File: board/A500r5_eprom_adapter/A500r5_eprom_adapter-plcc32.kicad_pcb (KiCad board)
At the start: 2 copper layers, 10 parts, among them J1 PWR, J2 A18 Selector, J3 A19 Selector, U1 27C400-A500, U2 27C080-L, U3 27C080-L

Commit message: More PLCC32 changes
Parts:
- U2: moved to F.Cu
- moved U2 17.8 mm to (141.0, 96.5)
- moved U3 14.2 mm to (141.0, 96.5)
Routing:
- net VCC: track 0.00 -> 25.7 mm, vias 0 -> 1
- net /A7: track 0.00 -> 16.3 mm, vias 0 -> 1
- net /A14: track 0.00 -> 15.6 mm, vias 0 -> 1
- net /A16: track 0.00 -> 15.4 mm, vias 0 -> 1
- net /A19: track 0.00 -> 13.7 mm, vias 0 -> 1
- net /A18: track 0.00 -> 13.7 mm, vias 0 -> 1
- net /A17: track 0.00 -> 13.7 mm, vias 0 -> 1
- net /A15: track 0.00 -> 13.7 mm, vias 0 -> 1
- net /A12: track 0.00 -> 13.7 mm, vias 0 -> 1
- net /A6: track 0.00 -> 13.0 mm, vias 0 -> 1
- net /A13: track 0.00 -> 13.0 mm, vias 0 -> 1
- net /A8: track 0.00 -> 9.68 mm, vias 0 -> 1
- net /A5: track 0.00 -> 9.68 mm, vias 0 -> 1
- net /A9: track 0.00 -> 7.14 mm, vias 0 -> 1
- net /A4: track 0.00 -> 7.14 mm, vias 0 -> 1
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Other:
- net class POWER added: clearance 0.2, trace_width 0.35, via_dia 0.8, via_drill 0.4

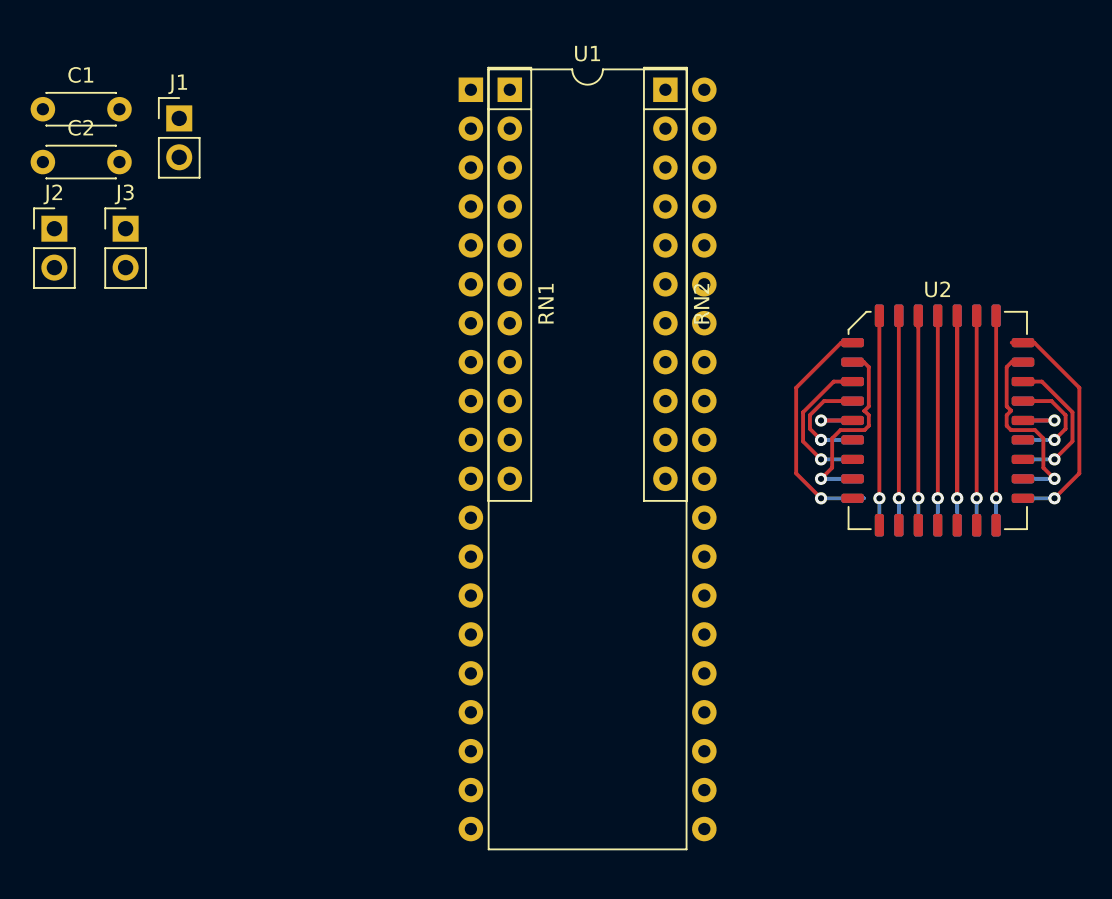
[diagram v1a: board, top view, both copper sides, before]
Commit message: Add more PLCC32 tracks
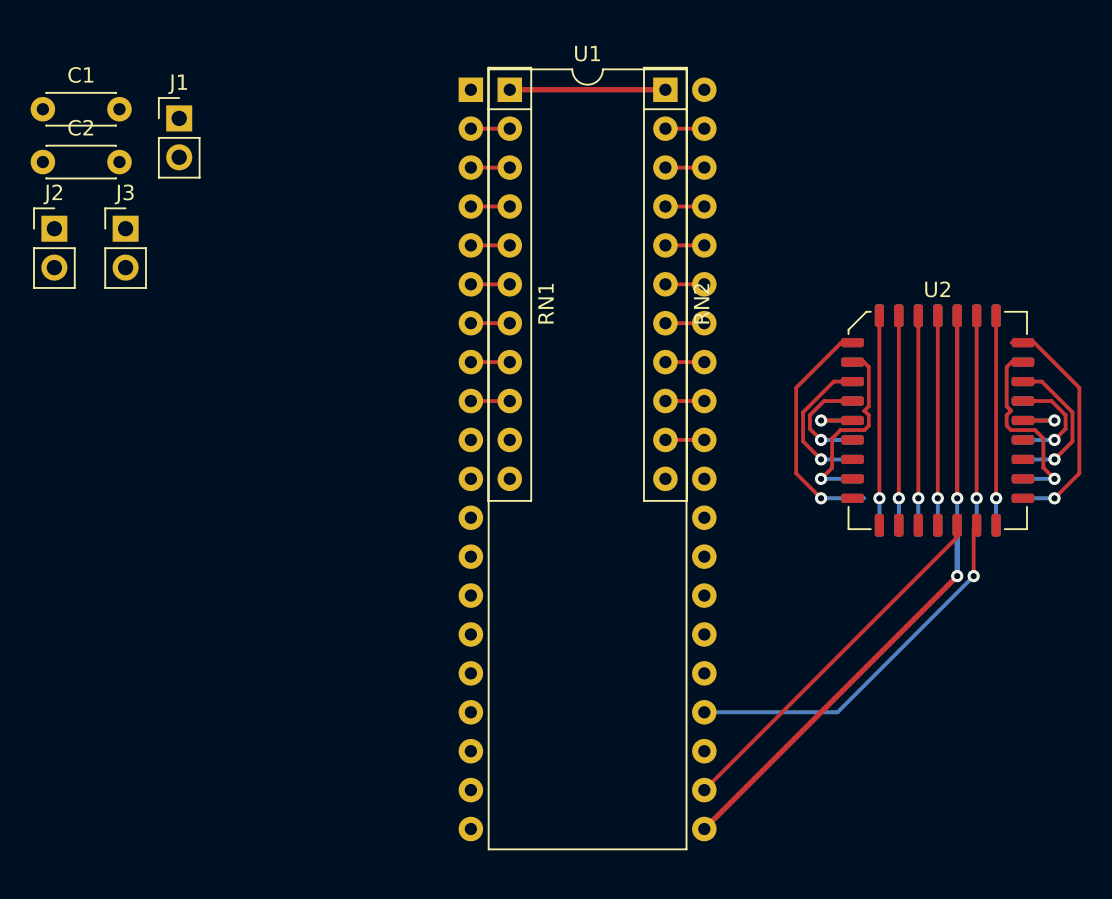
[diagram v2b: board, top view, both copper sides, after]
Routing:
- net VCC: track 25.7 -> 62.6 mm, vias 1 -> 2
- net /D5-L: track 0.00 -> 24.7 mm, vias 0 -> 1
- net /D4-L: track 0.00 -> 24.1 mm
- net /A7: track 16.3 -> 18.9 mm
- net /A6: track 13.0 -> 15.6 mm
- net /A5: track 9.68 -> 12.2 mm
- net /A3: track 4.12 -> 6.66 mm
- net /A2: track 0.00 -> 2.54 mm
- net /A17: track 13.7 -> 16.2 mm
- net /A16: track 15.4 -> 18.0 mm
- net /A15: track 13.7 -> 16.2 mm
- net /A13: track 13.0 -> 15.5 mm
- net /A12: track 13.7 -> 16.2 mm
- net /A11: track 4.12 -> 6.66 mm
- net /A10: track 0.00 -> 2.54 mm
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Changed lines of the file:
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@@
     (thickness 1.6)
     (drawings 0)
-    (tracks 100)
+    (tracks 129)
     (zones 0)
     (modules 10)
@@
   (segment (start 142.24 101.6) (end 142.24 89.543232) (width 0.25) (layer F.Cu) (net 2))
   (segment (start 142.24 101.6) (end 142.24 103.3575) (width 0.25) (layer B.Cu) (net 2))
+  (segment (start 113.03 74.93) (end 123.19 74.93) (width 0.35) (layer F.Cu) (net 2))
+  (segment (start 125.73 123.19) (end 142.24 106.68) (width 0.35) (layer F.Cu) (net 2))
+  (via (at 142.24 106.68) (size 0.8) (drill 0.4) (layers F.Cu B.Cu) (net 2))
+  (segment (start 142.24 106.68) (end 142.24 103.3575) (width 0.35) (layer B.Cu) (net 2))
   (via (at 143.51 101.6) (size 0.8) (drill 0.4) (layers F.Cu B.Cu) (net 3))
   (segment (start 143.51 89.6825) (end 143.51 101.6) (width 0.25) (layer F.Cu) (net 3))
@@
   (segment (start 149.76501 97.88499) (end 149.76501 95.985598) (width 0.25) (layer F.Cu) (net 5))
   (segment (start 148.59 99.06) (end 149.76501 97.88499) (width 0.25) (layer F.Cu) (net 5))
+  (segment (start 113.03 95.25) (end 110.49 95.25) (width 0.25) (layer F.Cu) (net 6))
+  (segment (start 113.03 92.71) (end 110.49 92.71) (width 0.25) (layer F.Cu) (net 7))
+  (segment (start 113.03 90.17) (end 110.49 90.17) (width 0.25) (layer F.Cu) (net 8))
   (segment (start 135.4075 96.52) (end 133.35 96.52) (width 0.25) (layer F.Cu) (net 9))
   (via (at 133.35 96.52) (size 0.8) (drill 0.4) (layers F.Cu B.Cu) (net 9))
   (segment (start 133.35 96.52) (end 135.4075 96.52) (width 0.25) (layer B.Cu) (net 9))
+  (segment (start 113.03 87.63) (end 110.49 87.63) (width 0.25) (layer F.Cu) (net 9))
   (segment (start 135.4075 97.79) (end 133.35 97.79) (width 0.25) (layer B.Cu) (net 10))
   (via (at 133.35 97.79) (size 0.8) (drill 0.4) (layers F.Cu B.Cu) (net 10))
@@
   (segment (start 132.624999 97.064999) (end 132.624999 96.171999) (width 0.25) (layer F.Cu) (net 10))
   (segment (start 133.35 97.79) (end 132.624999 97.064999) (width 0.25) (layer F.Cu) (net 10))
+  (segment (start 113.03 85.09) (end 110.49 85.09) (width 0.25) (layer F.Cu) (net 10))
   (segment (start 135.4075 99.06) (end 133.35 99.06) (width 0.25) (layer B.Cu) (net 11))
   (via (at 133.35 99.06) (size 0.8) (drill 0.4) (layers F.Cu B.Cu) (net 11))
@@
   (segment (start 134.67 93.98) (end 135.4075 93.98) (width 0.25) (layer F.Cu) (net 11))
   (segment (start 133.35 99.06) (end 132.17499 97.88499) (width 0.25) (layer F.Cu) (net 11))
+  (segment (start 113.03 82.55) (end 110.49 82.55) (width 0.25) (layer F.Cu) (net 11))
   (segment (start 135.4075 100.33) (end 133.35 100.33) (width 0.25) (layer B.Cu) (net 12))
   (via (at 133.35 100.33) (size 0.8) (drill 0.4) (layers F.Cu B.Cu) (net 12))
@@
   (segment (start 134.075001 99.604999) (end 134.075001 97.693251) (width 0.25) (layer F.Cu) (net 12))
   (segment (start 133.35 100.33) (end 134.075001 99.604999) (width 0.25) (layer F.Cu) (net 12))
+  (segment (start 113.03 80.01) (end 110.49 80.01) (width 0.25) (layer F.Cu) (net 12))
   (via (at 133.35 101.6) (size 0.8) (drill 0.4) (layers F.Cu B.Cu) (net 13))
   (segment (start 135.4075 101.6) (end 136.145 101.6) (width 0.25) (layer B.Cu) (net 13))
@@
   (segment (start 131.72498 99.97498) (end 131.72498 94.38502) (width 0.25) (layer F.Cu) (net 13))
   (segment (start 133.35 101.6) (end 131.72498 99.97498) (width 0.25) (layer F.Cu) (net 13))
+  (segment (start 113.03 77.47) (end 110.49 77.47) (width 0.25) (layer F.Cu) (net 13))
   (via (at 144.78 101.6) (size 0.8) (drill 0.4) (layers F.Cu B.Cu) (net 14))
   (segment (start 144.78 89.6825) (end 144.78 101.6) (width 0.25) (layer F.Cu) (net 14))
   (segment (start 144.78 101.6) (end 144.78 103.3575) (width 0.25) (layer B.Cu) (net 14))
+  (segment (start 123.19 97.79) (end 125.73 97.79) (width 0.25) (layer F.Cu) (net 14))
   (segment (start 139.7 89.6825) (end 139.7 90.42) (width 0.25) (layer F.Cu) (net 15))
   (via (at 139.7 101.6) (size 0.8) (drill 0.4) (layers F.Cu B.Cu) (net 15))
@@
   (segment (start 139.7 89.543232) (end 139.7 101.6) (width 0.25) (layer F.Cu) (net 15))
   (segment (start 139.7 101.6) (end 139.7 103.3575) (width 0.25) (layer B.Cu) (net 15))
+  (segment (start 123.19 95.25) (end 125.73 95.25) (width 0.25) (layer F.Cu) (net 15))
   (segment (start 138.43 89.6825) (end 138.43 101.6) (width 0.25) (layer F.Cu) (net 16))
   (via (at 138.43 101.6) (size 0.8) (drill 0.4) (layers F.Cu B.Cu) (net 16))
   (segment (start 138.43 101.6) (end 138.43 103.3575) (width 0.25) (layer B.Cu) (net 16))
+  (segment (start 123.19 92.71) (end 125.73 92.71) (width 0.25) (layer F.Cu) (net 16))
   (segment (start 146.5325 91.44) (end 145.795 91.44) (width 0.25) (layer F.Cu) (net 17))
   (via (at 148.59 101.6) (size 0.8) (drill 0.4) (layers F.Cu B.Cu) (net 17))
@@
   (segment (start 150.21502 94.38502) (end 147.27 91.44) (width 0.25) (layer F.Cu) (net 17))
   (segment (start 148.59 101.6) (end 150.21502 99.97498) (width 0.25) (layer F.Cu) (net 17))
+  (segment (start 123.19 90.17) (end 125.73 90.17) (width 0.25) (layer F.Cu) (net 17))
   (segment (start 146.5325 100.33) (end 148.59 100.33) (width 0.25) (layer B.Cu) (net 18))
   (via (at 148.59 100.33) (size 0.8) (drill 0.4) (layers F.Cu B.Cu) (net 18))
@@
   (segment (start 147.864999 99.604999) (end 147.864999 97.693251) (width 0.25) (layer F.Cu) (net 18))
   (segment (start 148.59 100.33) (end 147.864999 99.604999) (width 0.25) (layer F.Cu) (net 18))
+  (segment (start 123.19 87.63) (end 125.73 87.63) (width 0.25) (layer F.Cu) (net 18))
   (segment (start 137.16 89.6825) (end 137.16 101.6) (width 0.25) (layer F.Cu) (net 19))
   (via (at 137.16 101.6) (size 0.8) (drill 0.4) (layers F.Cu B.Cu) (net 19))
   (segment (start 137.16 101.6) (end 137.16 103.3575) (width 0.25) (layer B.Cu) (net 19))
+  (segment (start 123.19 85.09) (end 125.73 85.09) (width 0.25) (layer F.Cu) (net 19))
   (segment (start 146.5325 96.52) (end 148.59 96.52) (width 0.25) (layer B.Cu) (net 20))
   (via (at 148.59 96.52) (size 0.8) (drill 0.4) (layers F.Cu B.Cu) (net 20))
   (segment (start 148.59 96.52) (end 146.5325 96.52) (width 0.25) (layer F.Cu) (net 20))
+  (segment (start 123.19 82.55) (end 125.73 82.55) (width 0.25) (layer F.Cu) (net 20))
+  (segment (start 123.19 80.01) (end 125.73 80.01) (width 0.25) (layer F.Cu) (net 21))
   (segment (start 146.5325 97.79) (end 148.59 97.79) (width 0.25) (layer B.Cu) (net 22))
   (via (at 148.59 97.79) (size 0.8) (drill 0.4) (layers F.Cu B.Cu) (net 22))
@@
   (segment (start 149.315001 97.064999) (end 149.315001 96.171999) (width 0.25) (layer F.Cu) (net 22))
   (segment (start 148.59 97.79) (end 149.315001 97.064999) (width 0.25) (layer F.Cu) (net 22))
+  (segment (start 123.19 77.47) (end 125.73 77.47) (width 0.25) (layer F.Cu) (net 22))
+  (segment (start 134.423002 115.57) (end 143.313002 106.68) (width 0.25) (layer B.Cu) (net 38))
+  (segment (start 125.73 115.57) (end 134.423002 115.57) (width 0.25) (layer B.Cu) (net 38))
+  (segment (start 143.313002 106.68) (end 143.313002 106.68) (width 0.25) (layer B.Cu) (net 38))
+  (via (at 143.313002 106.68) (size 0.8) (drill 0.4) (layers F.Cu B.Cu) (net 38))
+  (segment (start 143.313002 103.554498) (end 143.51 103.3575) (width 0.25) (layer F.Cu) (net 38))
+  (segment (start 143.313002 106.68) (end 143.313002 103.554498) (width 0.25) (layer F.Cu) (net 38))
+  (segment (start 142.24 104.14) (end 142.24 103.3575) (width 0.25) (layer F.Cu) (net 40))
+  (segment (start 125.73 120.65) (end 142.24 104.14) (width 0.25) (layer F.Cu) (net 40))
 )

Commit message: More tracks
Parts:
- moved U2 16.7 mm to (138.4, 113.0)
- moved U3 16.7 mm to (138.4, 113.0)
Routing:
- net /D1-L: track 0.00 -> 31.7 mm
- net /D3-L: track 0.00 -> 30.1 mm, vias 0 -> 2
- net /D2-L: track 0.00 -> 28.3 mm, vias 0 -> 1
- net VCC: track 62.6 -> 41.5 mm
- net /A16: track 18.0 -> 34.4 mm
- net /D4-L: track 24.1 -> 17.3 mm
- net /D5-L: track 24.7 -> 25.3 mm

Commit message: Add changes and add gerbers
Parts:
- removed J1: PWR, Connector_PinHeader_2.54mm:PinHeader_1x02_P2.54mm_Vertical
- C1, C2: footprint Capacitor_THT:C_Disc_D4.3mm_W1.9mm_P5.00mm -> Capacitor_SMD:C_1206_3216Metric
- U2: moved to B.Cu
- moved C1 67.6 mm to (138.4, 114.3), turned to 270 degrees
- moved J2 58.1 mm to (139.7, 97.8), turned to 270 degrees
- moved C2 56.0 mm to (138.4, 83.8), turned to 270 degrees
- moved J3 54.3 mm to (139.7, 100.3), turned to 270 degrees
- moved U2 29.2 mm to (138.4, 83.8), turned to 180 degrees
- moved U3 1.27 mm to (138.4, 114.3), turned to 180 degrees
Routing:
- net /A6: track 15.6 -> 86.0 mm, vias 1 -> 0
- net GND: track 0.00 -> 67.5 mm, vias 0 -> 2
- net /A7: track 18.9 -> 79.3 mm
- net /A8: track 9.68 -> 69.6 mm, vias 1 -> 0
- net /A0: track 2.54 -> 40.4 mm
- net /A1: track 2.54 -> 40.4 mm, vias 0 -> 2
- net /A2: track 2.54 -> 36.9 mm, vias 0 -> 2
- net /A16: track 34.4 -> 2.54 mm, vias 1 -> 0
- net /D1-L: track 31.7 -> 0.00 mm
- net /A5: track 12.2 -> 43.3 mm, vias 1 -> 2
- net /D3-H: track 0.00 -> 30.9 mm
- net /D3-L: track 30.1 -> 0.00 mm, vias 2 -> 0
- net /A12: track 16.2 -> 44.6 mm
- net /D2-L: track 28.3 -> 0.00 mm, vias 1 -> 0
- net /A3: track 6.66 -> 34.6 mm, vias 1 -> 2
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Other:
- board outline added: 40.6 x 54.6 mm

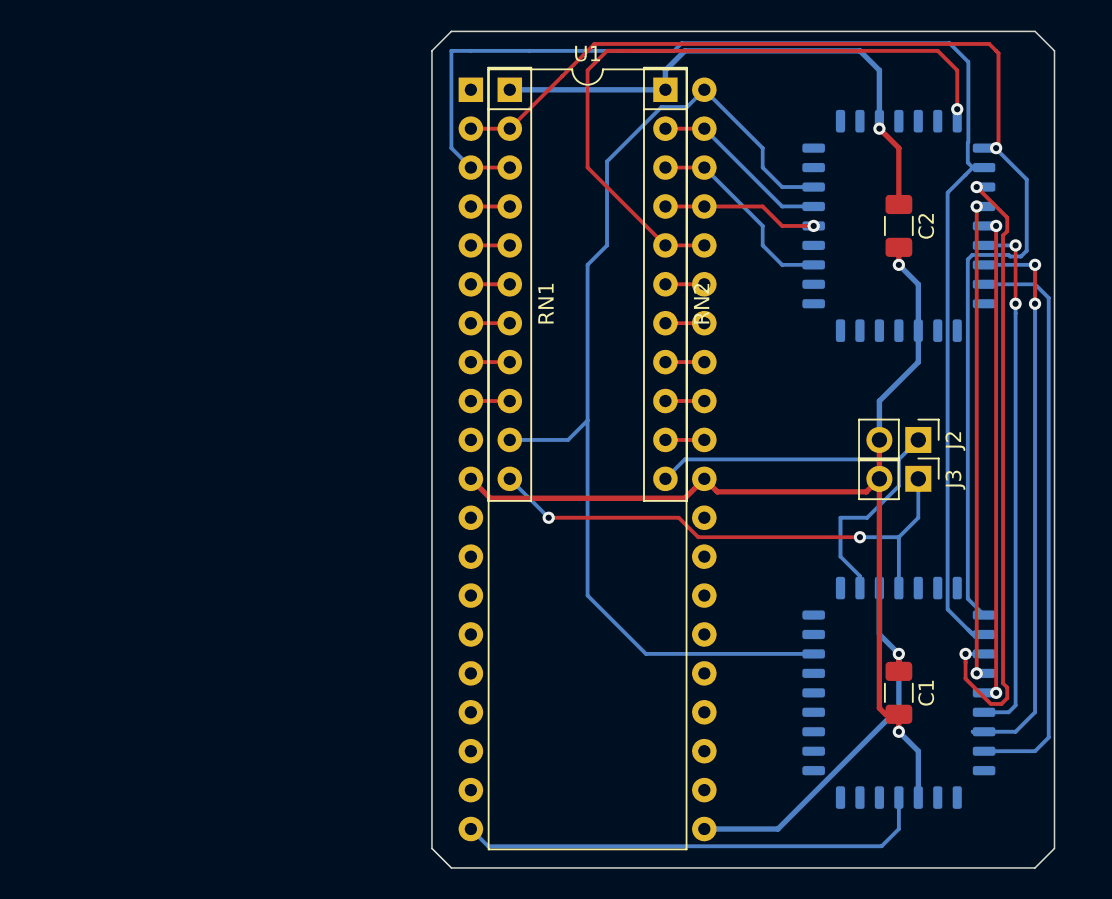
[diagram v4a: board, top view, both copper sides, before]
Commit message: Add more board variants
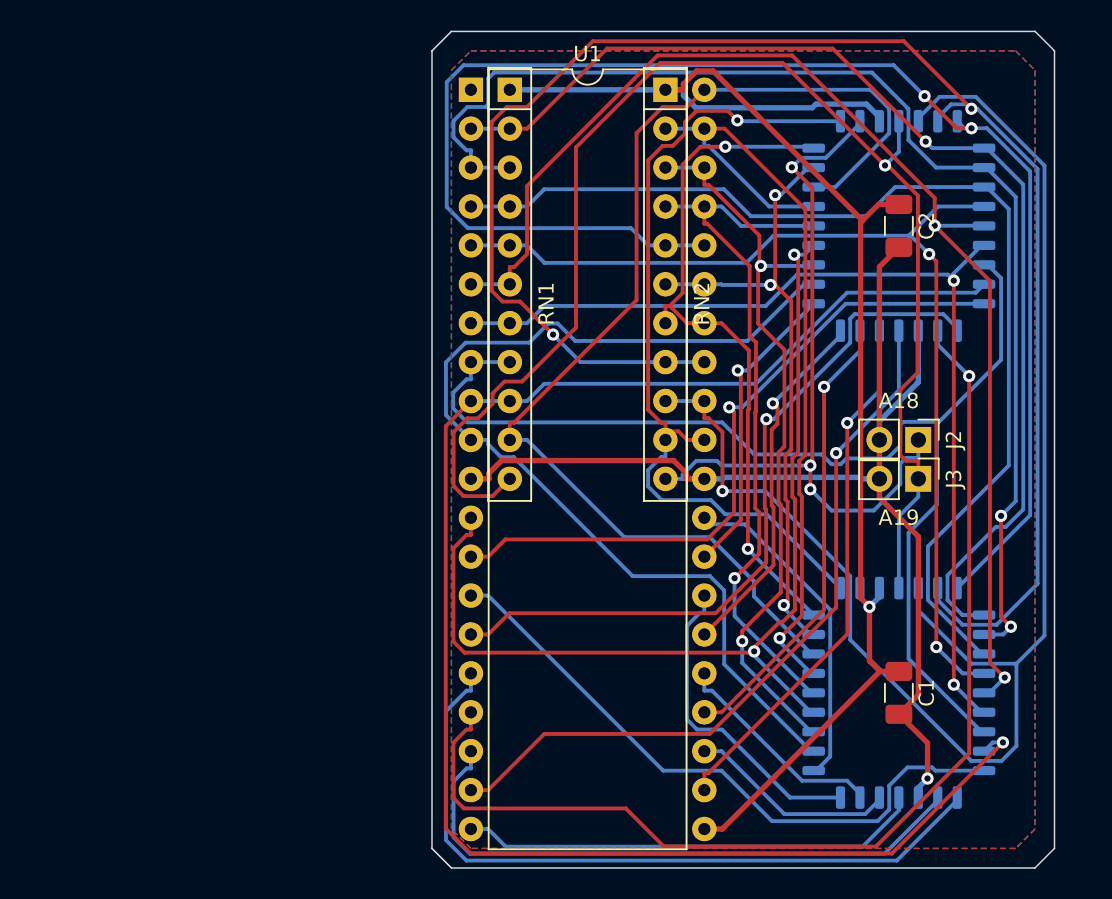
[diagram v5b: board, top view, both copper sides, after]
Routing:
- net /A15: track 2.54 -> 107.2 mm, vias 0 -> 2
- net /A16: track 2.54 -> 97.2 mm, vias 0 -> 1
- net /D2-L: track 0.00 -> 72.2 mm, vias 0 -> 1
- net /~CE: track 0.00 -> 66.6 mm
- net /A0: track 40.4 -> 106.8 mm, vias 0 -> 1
- net /~OE: track 0.00 -> 63.3 mm, vias 0 -> 2
- net /A19: track 34.6 -> 89.9 mm, vias 2 -> 1
- net /A12: track 44.6 -> 97.7 mm, vias 1 -> 2
- net /A17: track 2.54 -> 55.2 mm, vias 0 -> 1
- net /D3-L: track 0.00 -> 48.5 mm, vias 0 -> 1
- net /D1-H: track 0.00 -> 47.5 mm
- net /D1-L: track 0.00 -> 47.4 mm, vias 0 -> 1
- net /A3: track 34.6 -> 81.8 mm
- net /D0-L: track 0.00 -> 44.8 mm, vias 0 -> 1
- net /A14: track 2.54 -> 45.5 mm, vias 0 -> 2
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- added copper zone on B.Cu, net GND
- added copper zone on F.Cu, net GND
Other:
- board text added: "27C040/27C080"
- board text added: "A18"
- board text added: "A19"
- board text added: "HIGH"
- board text added: "LOW"
